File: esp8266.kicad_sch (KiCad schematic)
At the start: 12 parts, among them U1 ESP8266EX, U10 TS-1187A-B-A-B, U11 W25Q128JVSIQTR, U2 ESP8266EX, U3 AP2112K-3_3TRG1, U4 HDC1080DMBR, U5 MCP73831T-2ACI_OT, U6 MK-12C02-G020, U7 S2B-PH-SM4-TB(LF)(SN), U8 SK6812MINI-HS, U9 UMH3N

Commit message: Schematic done
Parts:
- removed U1: ESP8266EX, Package_DFN_QFN:QFN-32-1EP_5x5mm_P0.5mm_EP3.1x3.1mm_ThermalVias, symbol MCU_Espressif:ESP8266EX
- added AE1: Antenna_Shield, RF_Antenna:Texas_SWRA117D_2.4GHz_Right, symbol Device:Antenna_Shield
- added C1: 10u, jlc_footprints:C0603, symbol jlc_symbols:CL10A106KP8NNNC
- added C10, C2: 100n, jlc_footprints:C0603, symbol jlc_symbols:CC0603KRX7R9BB104
- added C3, C4: 10p, jlc_footprints:C0603, symbol jlc_symbols:CL10C100JB8NNNC
- added C5: 4.7u, jlc_footprints:C0603, symbol jlc_symbols:CL10A475KO8NNNC
- added C6: 5.6p, jlc_footprints:C0603, symbol jlc_symbols:CC0603BRNPO9BN5R6
- added C7: 1u, jlc_footprints:C0603, symbol jlc_symbols:CL10A105KB8NNNC
- added C9: 2.2u, jlc_footprints:C0603, symbol jlc_symbols:CL10A225KO8NNNC
- added D3: BAT20JFILM, jlc_footprints:SOD-323_L1.8-W1.3-LS2.5-RD, symbol jlc_symbols:BAT20JFILM
- added JP1: USB_B_Micro, jlc_footprints:MICRO-USB-SMD_1050171001, symbol Connector:USB_B_Micro
- added L1, L2: DNP, jlc_footprints:L0603, symbol jlc_symbols:SDFL1608S100KTF
- added OSHW1: github.com/besi/stepomatic, Symbol:OSHW-Symbol_6.7x6mm_SilkScreen, symbol Graphic:Logo_Open_Hardware_Small
- added Q1: AO3401A, jlc_footprints:SOT-23_L2.9-W1.3-P1.90-LS2.4-BR, symbol jlc_symbols:AO3401A
- added R1: 12k, jlc_footprints:R0603, symbol jlc_symbols:0603WAF1202T5E
- added R2: 200, jlc_footprints:R0603, symbol jlc_symbols:0603WAF2000T5E
- added R3, R5, R6, R7: 10k, jlc_footprints:R0603, symbol jlc_symbols:0603WAF1002T5E
- added R4: 2k, jlc_footprints:R0603, symbol jlc_symbols:0603WAF2001T5E
- added U13: CH340C, jlc_footprints:SOP-16_L10.0-W3.9-P1.27-LS6.0-BL, symbol Interface_USB:CH340C
- added Y1: 26Mhz, jlc_footprints:CRYSTAL-SMD_4P-L2.0-W1.6-BL, symbol jlc_symbols:Q22FA1280023012
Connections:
- net at U3.1 (VIN): now also U6.1, C7.2, D3.1 (K), Q1.2 (S)
- net GND: now reaches U3.2 (GND)
- net GND: now also REF1.0, REF1.1, U11.4 (GND), U2.33 (GND), U4.2 (GND), U4.7 (EP), U5.2 (VSS), U6.3, U7.1, U8.1 (GND), AE1.2 (Shield), C1.2, C10.1, C2.1, C3.1, C4.1, C5.1, C7.1, C9.1, JP1.5 (GND), JP1.6 (Shield), L1.1, L2.1, R1.1, R4.1, R6.2, R7.2, U13.1 (GND), Y1.2 (GND), Y1.4 (GND)
- net at U3.3 (EN): now also U6.2
- net +3V3: now reaches U3.5 (VOUT)
- net +3V3: now also REF1.2, U11.8 (VCC), U2.1 (VDDA), U2.11 (VDDPST), U2.17 (VDDPST), U2.29 (VDDD), U2.3 (VDD3P3), U2.30 (VDDA), U2.4 (VDD3P3), U4.5 (VDD), U8.3 (VDD), C1.1, C10.2, C2.2, C9.2, R3.1, R5.1, U13.16 (VCC), U13.4 (V3)
- net +BATT: now reaches U7.2
- net +BATT: now also U5.3 (VBAT), C5.2, Q1.3 (D)
- net GPIO2: now reaches REF1.3
- net GPIO2: now also U2.14 (GPIO2), U4.1 (SDA)
- net GPIO14: now reaches REF1.4
- net GPIO14: now also U2.9 (MTMS), U4.6 (SCL)
- net NEOPIXEL: now reaches U8.2 (DIN)
- net NEOPIXEL_OUT: now reaches U8.4 (DOUT)
- net DTR: now reaches U9.1 (E)
- net DTR: now also U9.5 (B), U13.13 (~{DTR})
- net RTS: now reaches U9.2 (B)
- net RTS: now also U9.4 (E), U13.14 (~{RTS})
- net RESET: now reaches U9.3 (C)
- net RESET: now also U2.32 (~{EXT_RSTB}), R5.2
- net GPIO0: now reaches U9.6 (C)
- net GPIO0: now also U2.15 (GPIO0)
- net SD_CS0: now reaches U11.1 (CS#)
- net SD_CS0: now also U2.20 (SDIO_CMD)
- net SD_SO: now reaches U11.2 (DO)
- net SD_SO: now also U2.22 (SDIO_DATA_0)
- net SD_WP: now reaches U11.3 (IO2)
- net SD_WP: now also U2.19 (SDIO_DATA_3)
- net SD_SI: now reaches U11.5 (DI)
- net SD_SI: now also U2.23 (SDIO_DATA_1)
- net SD_CLK: now reaches U11.6 (CLK)
- net SD_CLK: now also R2.2
- net SD_HD: now reaches U11.7 (IO3)
- net SD_HD: now also U2.18 (SDIO_DATA_2)
- net VBUS: now reaches U5.4 (VDD)
- net VBUS: now also D3.2 (A), JP1.1 (VBUS), Q1.1 (G), R7.1
- net at U5.5 (PROG): now also R4.2
- net GPIO12: now reaches U2.10 (MTDI)
- net GPIO13: now reaches U2.12 (MTCK)
- net GPIO15: now reaches U2.13 (MTDO)
- net GPIO15: now also R6.1
- net GPIO4: now reaches U2.16 (GPIO4)
- net LNA: now reaches U2.2 (LNA)
- net LNA: now also C6.1, L1.2
- net at U2.21 (SDIO_CLK): now also R2.1
- net GPIO5: now reaches U2.24 (GPIO5)
- net U0RXD: now reaches U2.25 (U0RXD)
- net U0RXD: now also U13.2 (TXD)
- net U0TXD: now reaches U2.26 (U0TXD)
- net U0TXD: now also U13.3 (RXD)
- net at U2.27 (XTAL_OUT): now also C3.2, Y1.3 (OSC2)
- net at U2.28 (XTAL_IN): now also C4.2, Y1.1 (OSC1)
- net at U2.31 (RES12K): now also R1.2
- net ADC: now reaches U2.6 (TOUT)
- net at U2.7 (CHIP_PU): now also R3.2
- net GPIO16: now reaches U2.8 (XPD_DCDC)
- new net: AE1.1 (A), C6.2, L2.2
- new net UD_N: JP1.2 (D-), U13.6 (UD-)
- new net UD_P: JP1.3 (D+), U13.5 (UD+)
- no-connect marks 0 -> 17
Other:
- note added: "USB + UART"
- moved on the sheet: U11, U3, U5, U6, U7, U8, U9

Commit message: Add antenna and layout the board
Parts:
- removed AE1: Antenna_Shield, RF_Antenna:Texas_SWRA117D_2.4GHz_Right, symbol Device:Antenna_Shield
- added C8: 100n, jlc_footprints:C0603, symbol jlc_symbols:CC0603KRX7R9BB104
- added E2: Antenna_Trace, RF_Antenna:Texas_SWRA117D_2.4GHz_Right, symbol Device:Antenna_Shield
- added J1, J2: Conn_01x08, Connector_PinHeader_2.54mm:PinHeader_1x08_P2.54mm_Vertical, symbol Connector_Generic:Conn_01x08
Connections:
- net NEOPIXEL is gone; now on net GPIO4: U8.2 (DIN)
- net +3V3: now also C8.2, J1.8 (Pin_8)
- net ADC: now also J1.2 (Pin_2)
- net GND: now also U10.3 (C), U10.4 (D), U6.1, C8.1, E2.2 (Shield), J2.7 (Pin_7); no longer U6.3
- net GPIO0: now also J2.5 (Pin_5)
- net GPIO12: now also J1.5 (Pin_5)
- net GPIO13: now also J1.6 (Pin_6)
- net GPIO14: now also J1.4 (Pin_4)
- net GPIO15: now also J1.7 (Pin_7)
- net GPIO16: now also J1.3 (Pin_3)
- net GPIO2: now also J2.6 (Pin_6)
- net GPIO4: now also J2.4 (Pin_4)
- net GPIO5: now also J2.3 (Pin_3)
- net RESET: now also U10.1 (A), J1.1 (Pin_1)
- net U0RXD: now also J2.2 (Pin_2)
- net U0TXD: now also J2.1 (Pin_1)
- net VBUS: now also J2.8 (Pin_8)
- net at C7.2, D3.1 (K), Q1.2 (S)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: now also U6.3; no longer U6.1
- net ANT: now reaches C6.2, L2.2
- net ANT: now also E2.1 (A)
- no-connect marks 17 -> 18

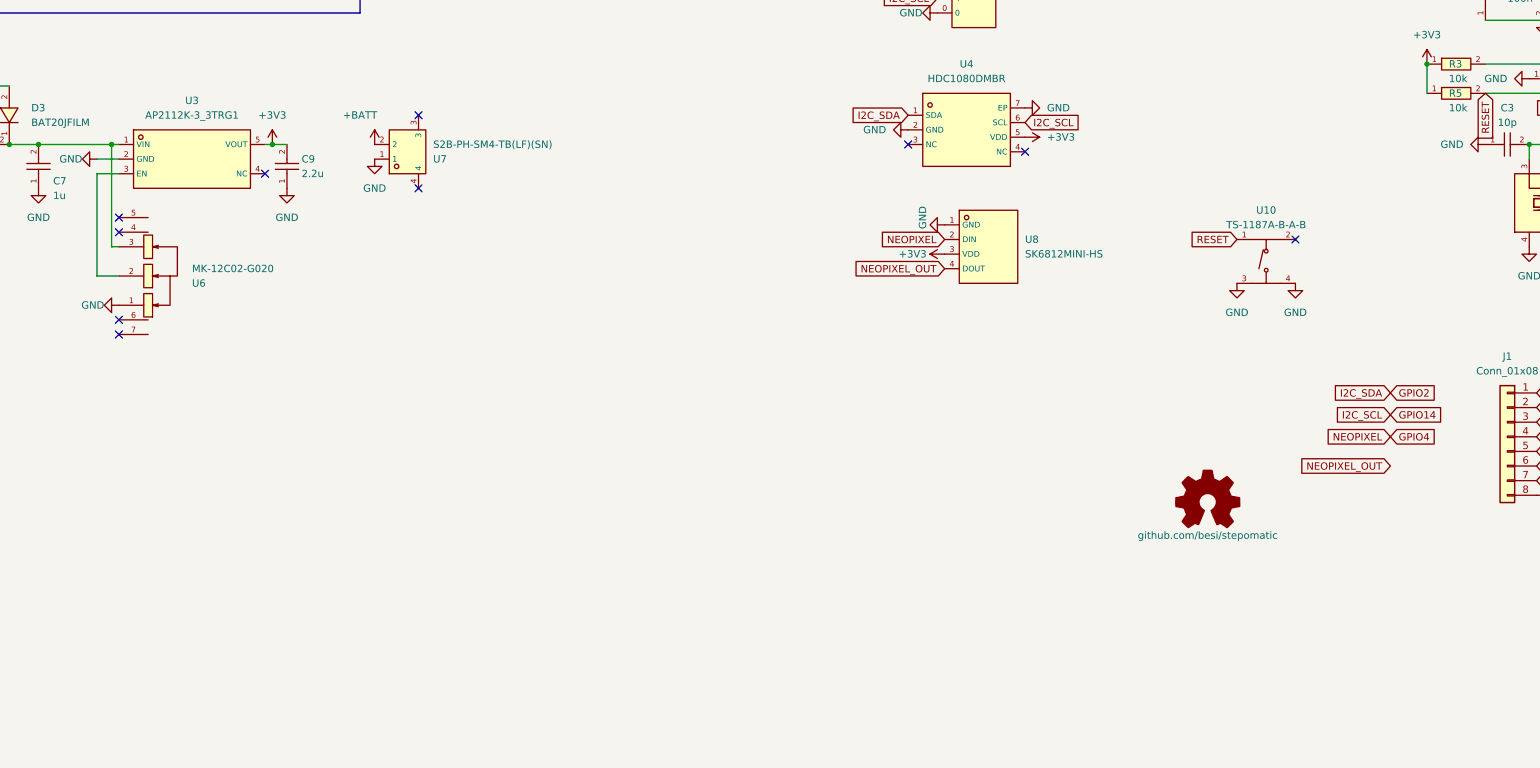
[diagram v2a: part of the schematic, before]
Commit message: Add silkscreen, test points and optional pull ups for I2C
Also don’t route underneath antenna pin
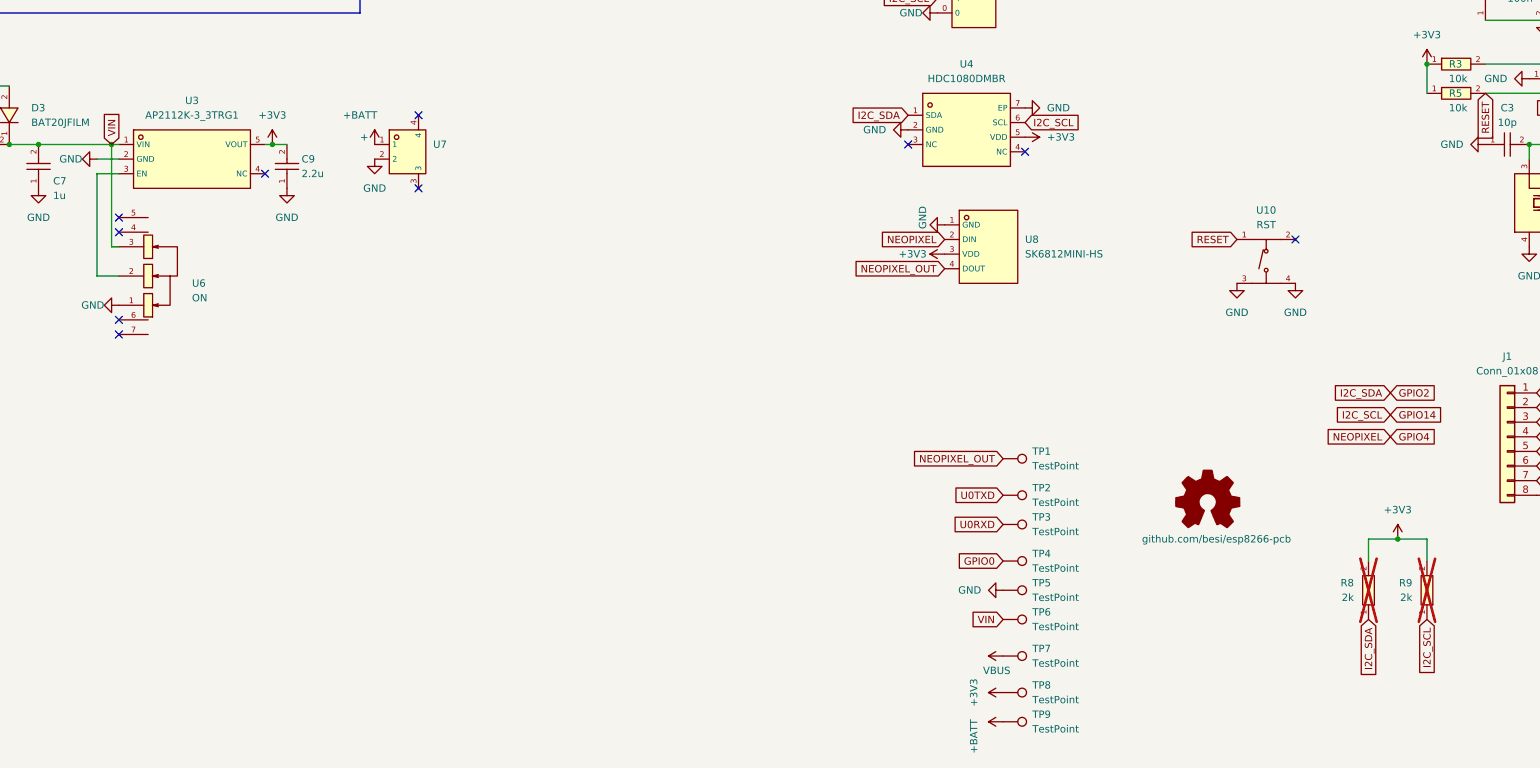
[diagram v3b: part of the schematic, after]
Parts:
- added R8, R9: 2k, Resistor_SMD:R_0603_1608Metric_Pad0.98x0.95mm_HandSolder, symbol jlc_symbols:0603WAF2001T5E
- added TP1, TP2, TP3, TP4, TP5, TP6, TP7, TP8, TP9: TestPoint, TestPoint:TestPoint_Pad_D1.0mm, symbol Connector:TestPoint
- OSHW1: value github.com/besi/stepomatic -> github.com/besi/esp8266-pcb; now left out of the parts list
- U10: value TS-1187A-B-A-B -> RST
- U6: value MK-12C02-G020 -> ON
- U7: value S2B-PH-SM4-TB(LF)(SN) -> +
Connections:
- net +3V3: now also R8.2, R9.2, TP8.1
- net +BATT: now also U7.1, TP9.1; no longer U7.2
- net GND: now also U7.2, TP5.1; no longer U7.1
- net GPIO0: now also TP4.1
- net GPIO14: now also R9.1
- net GPIO2: now also R8.1
- net NEOPIXEL_OUT: now also TP1.1
- net U0RXD: now also TP3.1
- net U0TXD: now also TP2.1
- net VBUS: now also TP7.1
- net VIN: now reaches C7.2, D3.1 (K), Q1.2 (S), U3.1 (VIN), U6.3
- net VIN: now also TP6.1

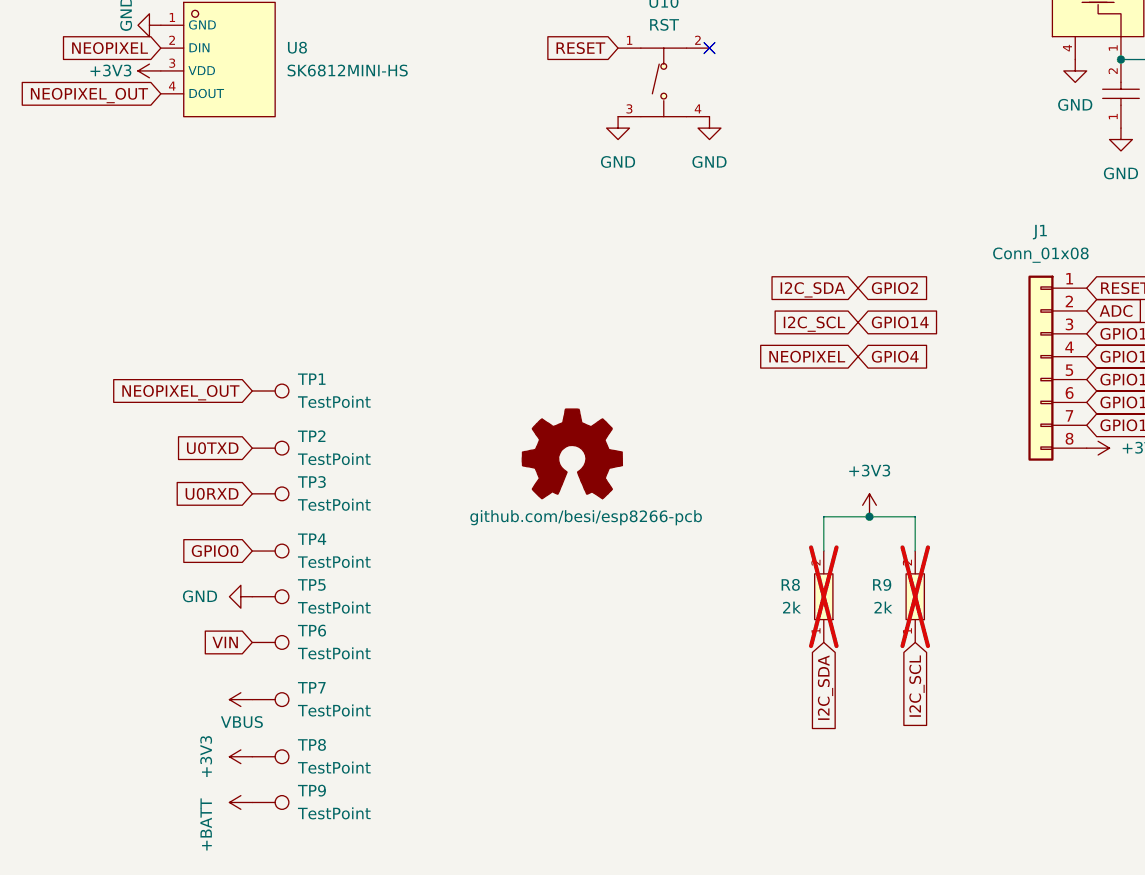
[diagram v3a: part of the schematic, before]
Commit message: Add a solder jumper for IO16 and RESET
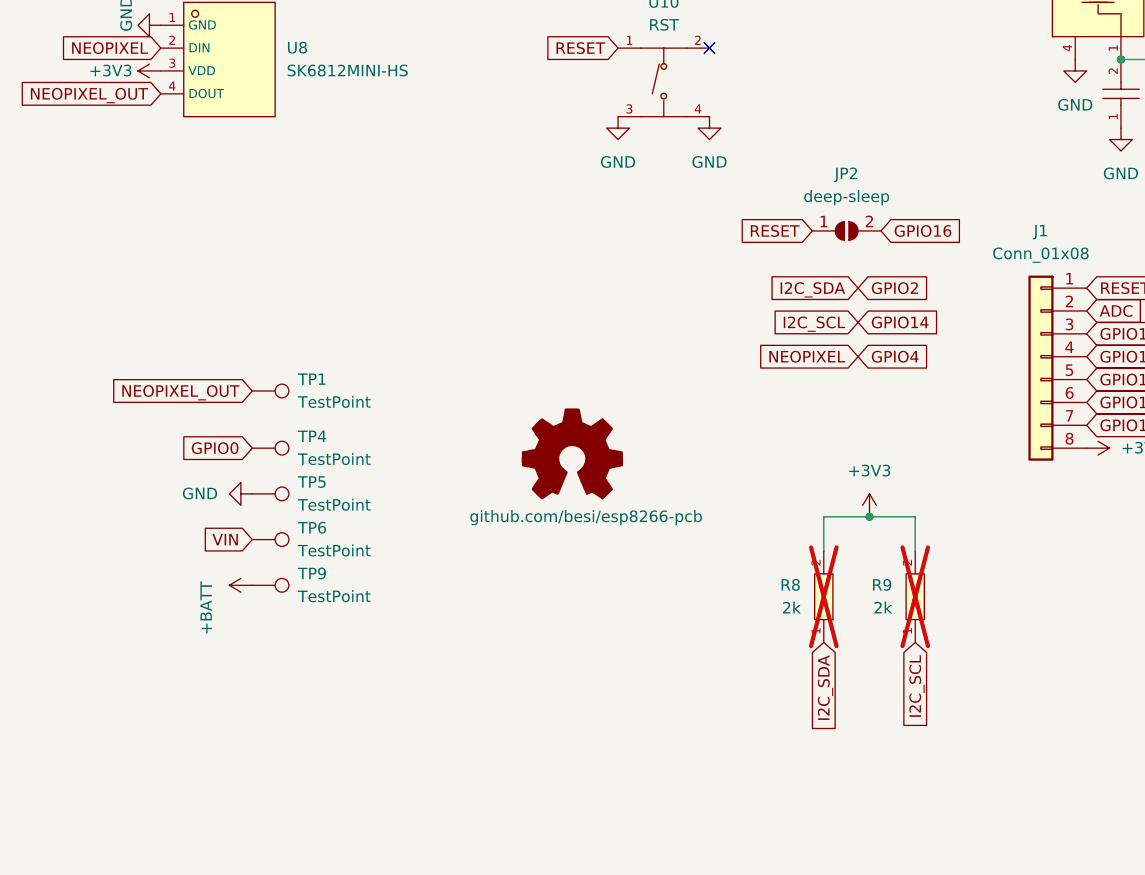
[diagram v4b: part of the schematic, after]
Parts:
- removed TP2, TP3, TP7, TP8: TestPoint, TestPoint:TestPoint_Pad_D1.0mm, symbol Connector:TestPoint
- added JP2: deep-sleep, Jumper:SolderJumper-2_P1.3mm_Open_TrianglePad1.0x1.5mm, symbol Jumper:SolderJumper_2_Open
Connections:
- net GPIO16: now also JP2.2 (B)
- net RESET: now also JP2.1 (A)
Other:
- moved on the sheet: TP4, TP5, TP6, TP9

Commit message: Prepare for production
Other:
- company: (none) -> Besmer Labs
- title: (none) -> ESP8266 Board
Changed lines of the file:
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@@
 (kicad_sch (version 20230121) (generator eeschema)
   (paper "A4")
+  (title_block
+    (title "ESP8266 Board")
+    (date "2024-03-29")
+    (rev "1.0")
+    (company "Besmer Labs")
+  )
   (junction (at -78.74 88.9) (diameter 0) (color 0 0 0 0)
   )

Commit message: Don’t add solder jumper to BOM
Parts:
- JP2: now left out of the parts list
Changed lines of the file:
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@@
   )
   (symbol (lib_id "Jumper:SolderJumper_2_Open") (at 142.24 125.73 0) (unit 1)
-    (in_bom yes) (on_board yes) (dnp no) (fields_autoplaced)
+    (in_bom no) (on_board yes) (dnp no) (fields_autoplaced)
     (property "Reference" "JP2" (at 142.24 119.38 0)
       (effects (font (size 1.27 1.27)))
